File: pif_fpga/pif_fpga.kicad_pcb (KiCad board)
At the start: 2 copper layers, 35 x 41 mm, 61 parts, among them P1 CONN_02X20, P2 CONN_01X18, P3 CONN_01X06, P4 CONN_01X05, U1 Si5351A, U2 LCMXO2-2000HC, U3 STM32F070CBT6, U4 W25Q128JVPIQ, U5 74LVC1G14, Y1 25 MHz

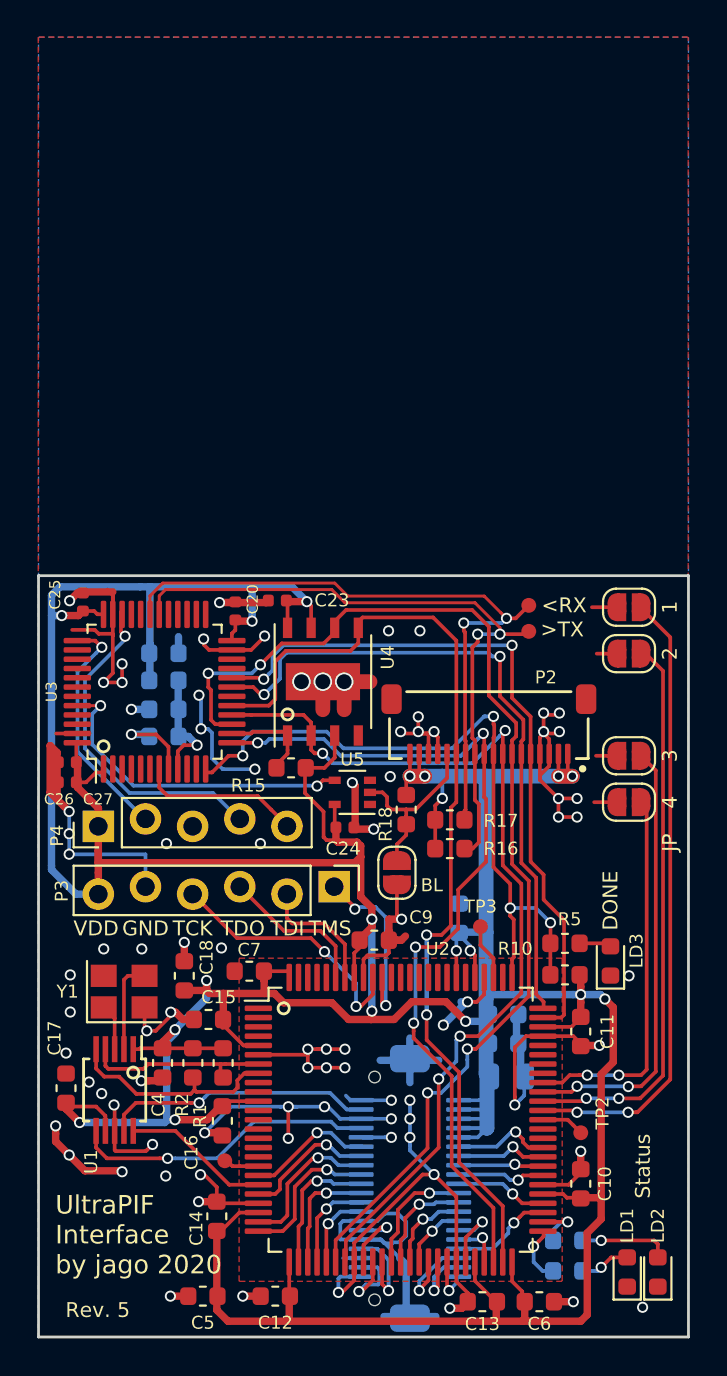
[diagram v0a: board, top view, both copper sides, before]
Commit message: changed connector to Hirose DF12
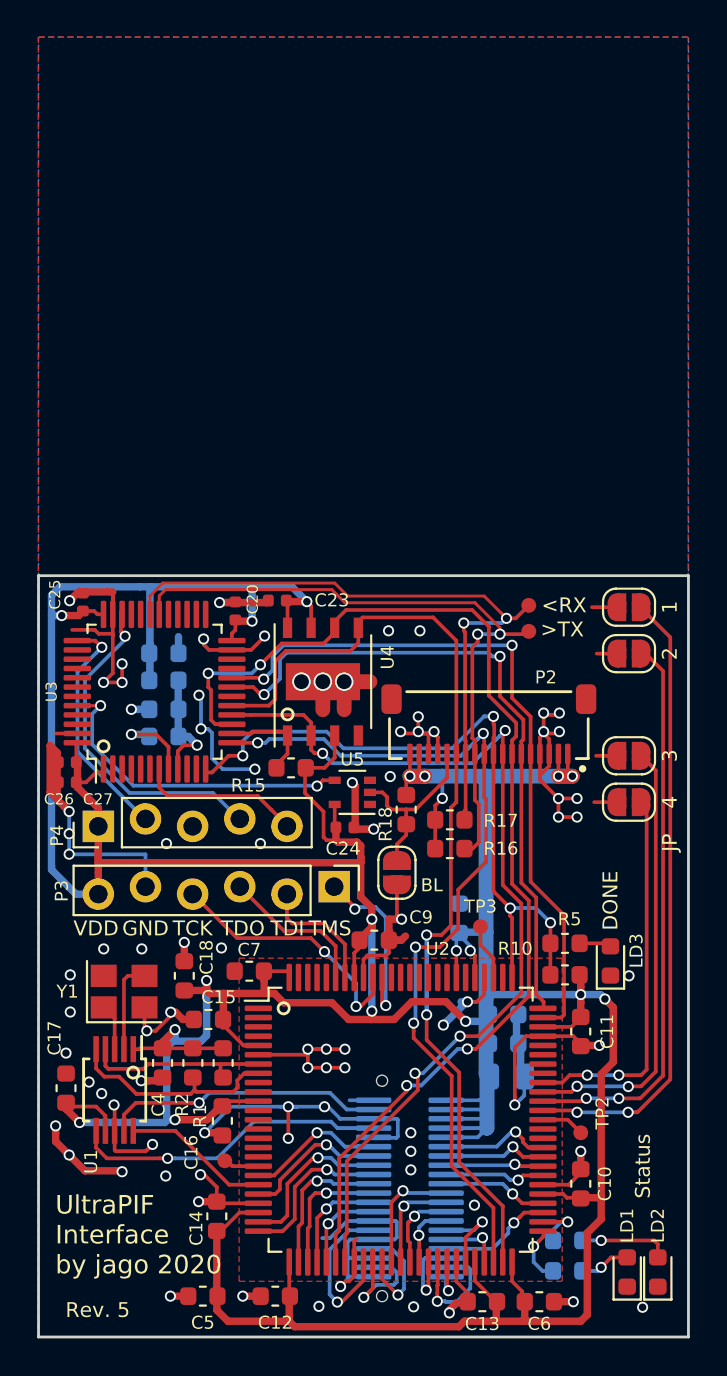
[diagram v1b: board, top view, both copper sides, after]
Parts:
- P1: footprint pif_fpga:Amphenol_MezzoStak-10106813_2x20x0.5mm -> pif_fpga:Hirose_DF12A-40DS-0.5V_2x20_P0.50mm_Vertical
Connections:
- P1 pad : GND -> (no net)
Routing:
- net GND: track 214.3 -> 184.6 mm, vias 87 -> 86
- net /CLK_PIF: track 3.93 -> 8.68 mm
- net /GREEN: track 3.76 -> 6.58 mm
- net +3V3: track 275.5 -> 277.6 mm
- net /DAT_PIF: track 4.91 -> 6.09 mm
- net /ADR_PIF: track 4.92 -> 5.99 mm
- net /P3_DAT_OUT: track 5.63 -> 6.57 mm
- net /P2_DAT_IN: track 4.63 -> 5.44 mm
- net /P2_DAT_OUT: track 3.54 -> 4.26 mm
- net /FPGA_MISO: track 50.6 -> 51.1 mm

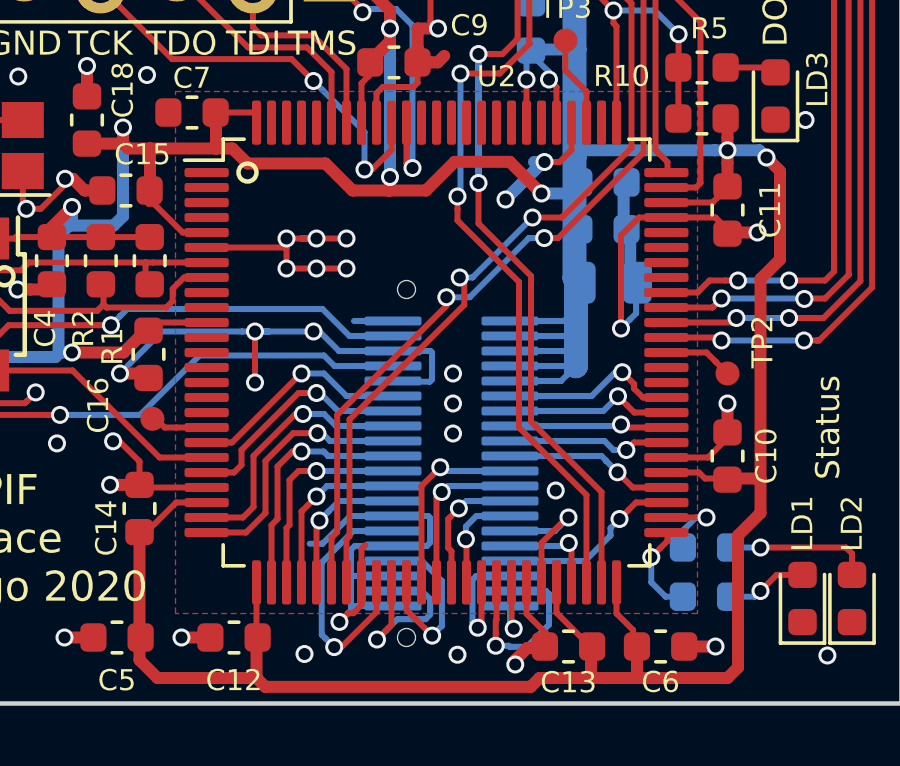
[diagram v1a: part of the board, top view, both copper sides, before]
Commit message: routing changes no copper fill under the connector
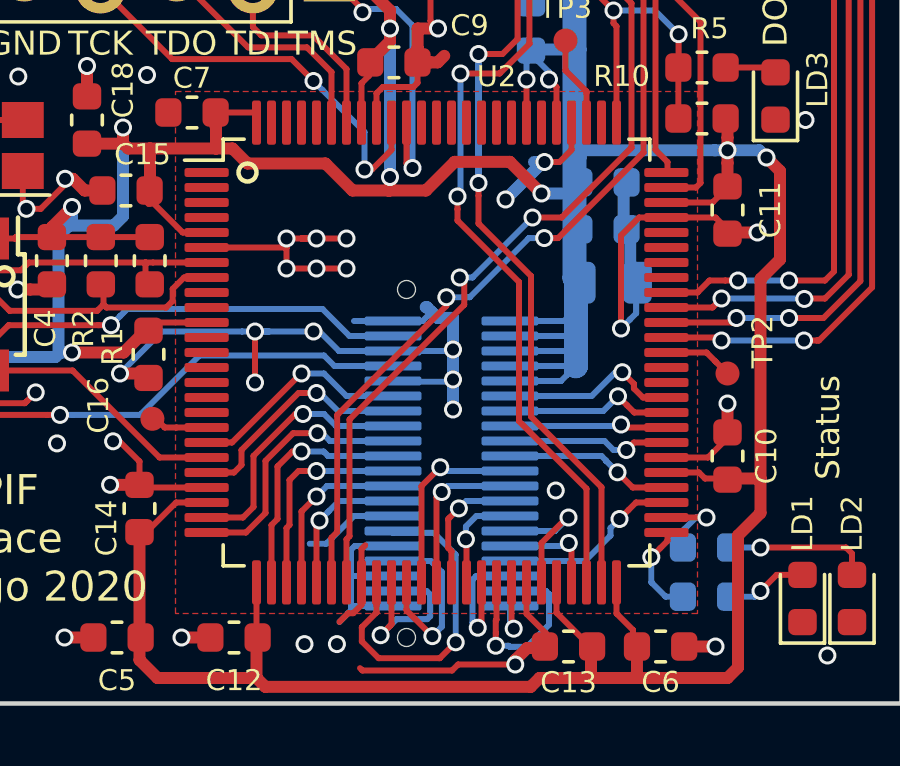
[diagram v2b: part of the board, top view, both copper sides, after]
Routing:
- net GND: track 184.6 -> 192.5 mm, vias 86 -> 85
- net /CLK_PIF: track 8.68 -> 11.1 mm

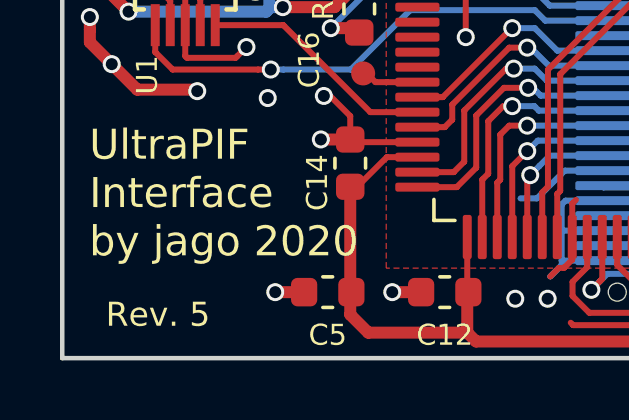
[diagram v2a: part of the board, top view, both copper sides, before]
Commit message: 'Rev 6' silk text
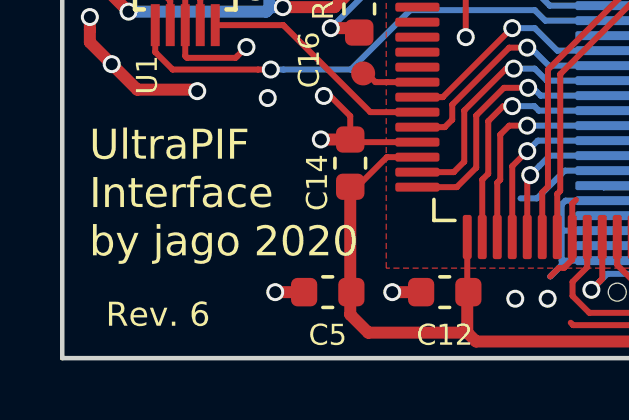
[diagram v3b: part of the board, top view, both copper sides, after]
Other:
- board text added: "Rev. 6"
- board text removed: "Rev. 5"
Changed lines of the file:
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@@
     (effects (font (size 0.8 0.8) (thickness 0.15)))
   )
-  (gr_text "Rev. 5" (at 146.45 138.55) (layer F.SilkS)
+  (gr_text "Rev. 6" (at 146.45 138.55) (layer F.SilkS)
     (effects (font (size 0.8 0.8) (thickness 0.15)) (justify left))
   )
